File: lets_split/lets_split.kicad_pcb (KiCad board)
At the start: 2 copper layers, 114.2 x 82 mm, 76 parts, among them P1 USB-rewire, P2 USB_OTG, P3 WS2812, P4 TRRS jack, SW1 SW_PUSH, SW10 SW_PUSH, SW11 SW_PUSH, SW12 SW_PUSH, SW13 SW_PUSH, SW14 SW_PUSH, SW15 SW_PUSH, SW16 SW_PUSH, SW17 SW_PUSH, SW18 SW_PUSH, SW19 SW_PUSH, SW2 SW_PUSH, SW20 SW_PUSH, SW21 SW_PUSH, SW22 SW_PUSH, SW23 SW_PUSH, SW24 SW_PUSH, SW3 SW_PUSH, SW4 SW_PUSH, SW5 SW_PUSH, SW6 SW_PUSH, SW7 SW_PUSH, SW8 SW_PUSH, SW9 SW_PUSH, U1 ArduinoProMicro

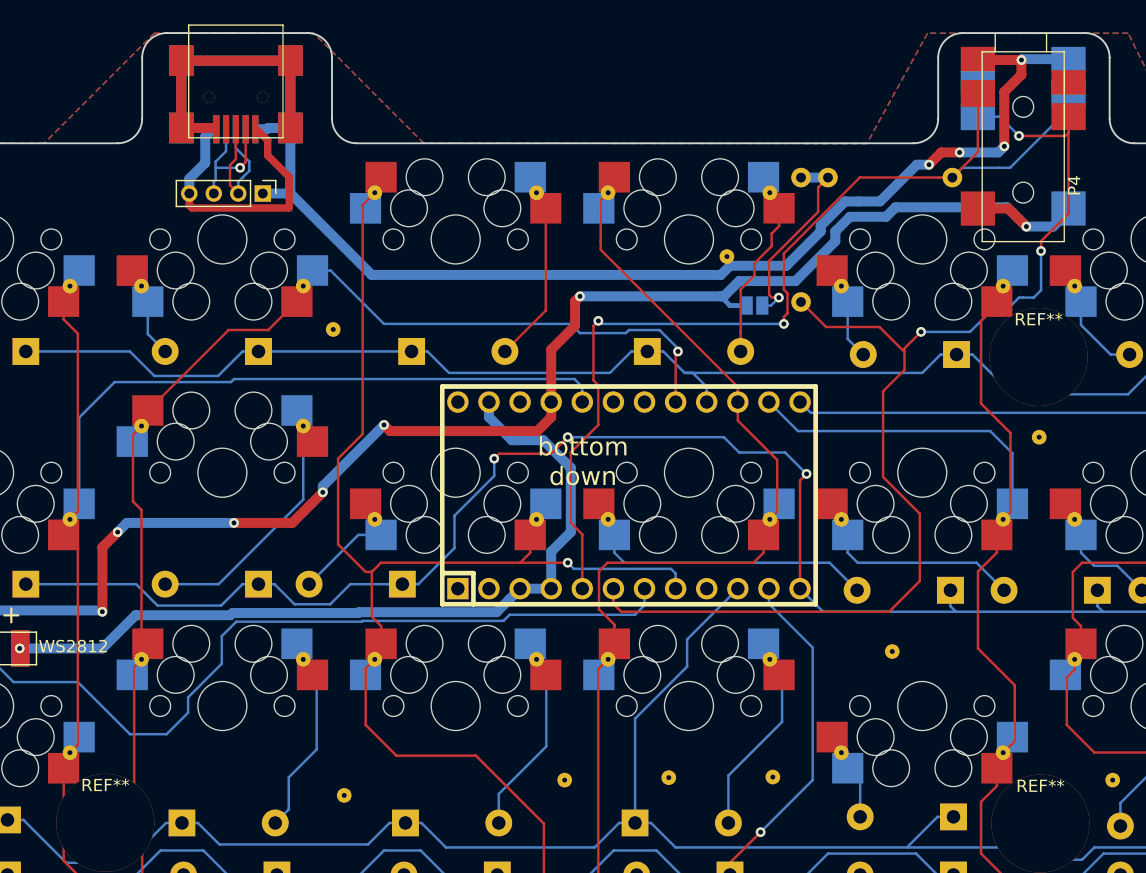
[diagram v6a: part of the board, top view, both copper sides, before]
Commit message: Updated schematic svg
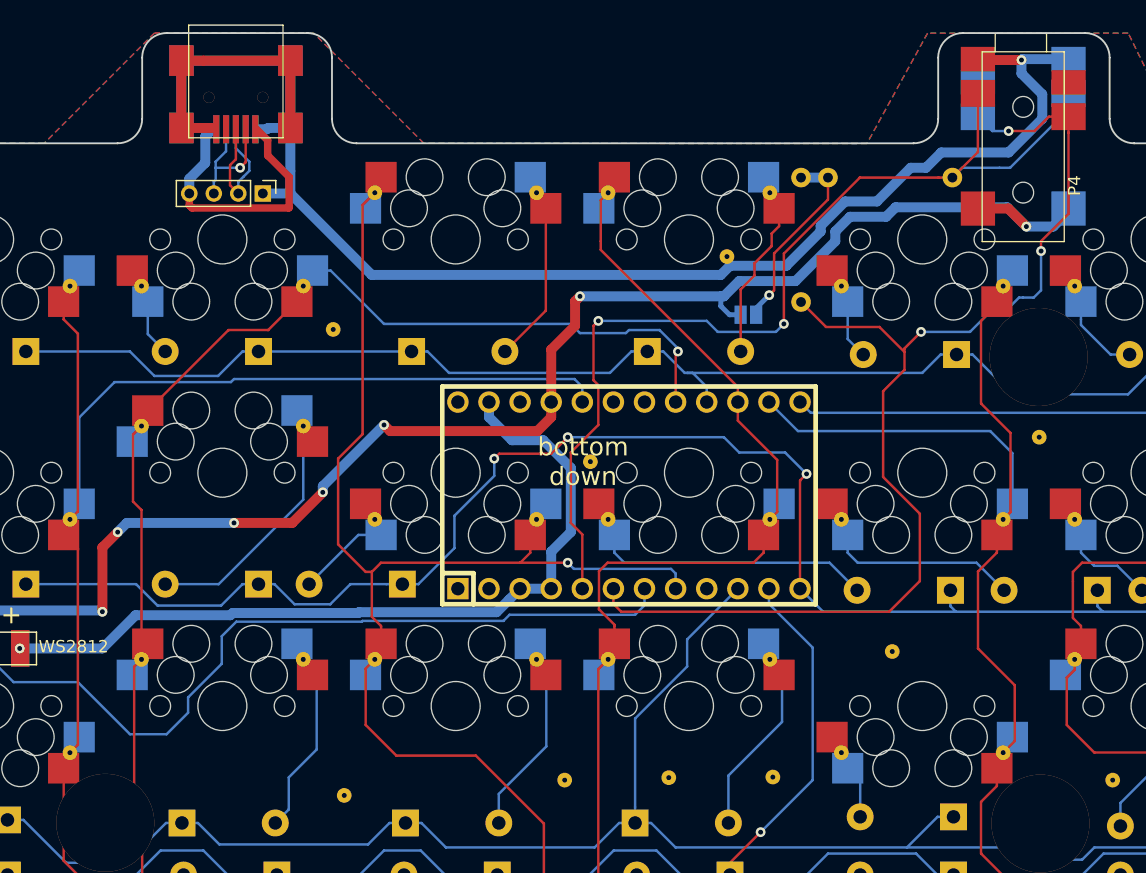
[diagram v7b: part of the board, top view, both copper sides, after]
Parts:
- added REF**: 1pin, Connect:1pin, F.Cu at (139.6, 91.0)
- moved JP1 0.90 mm to (152.5, 79.0)
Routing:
- net GND: track 199.1 -> 201.0 mm, vias 5 -> 2
- net VCC: track 124.1 -> 125.1 mm

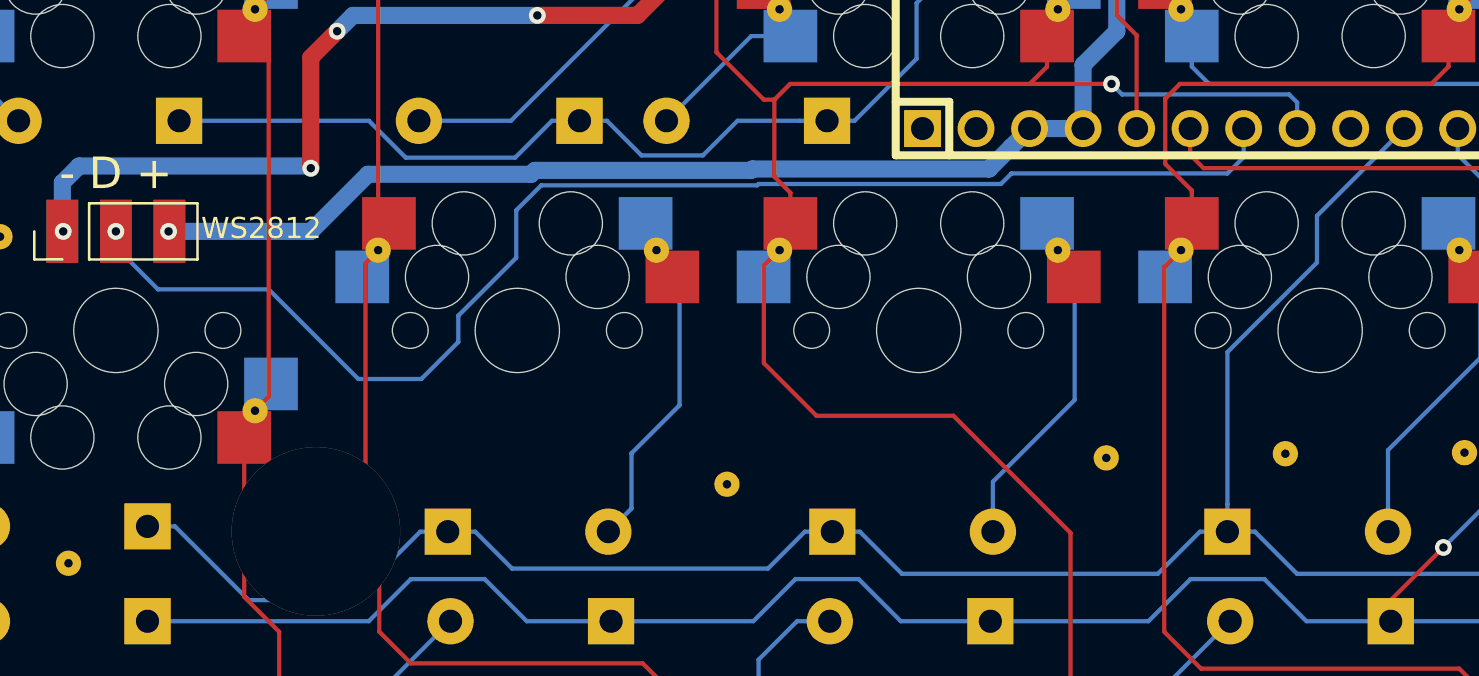
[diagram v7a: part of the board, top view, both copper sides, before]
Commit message: Added speaker output to the board
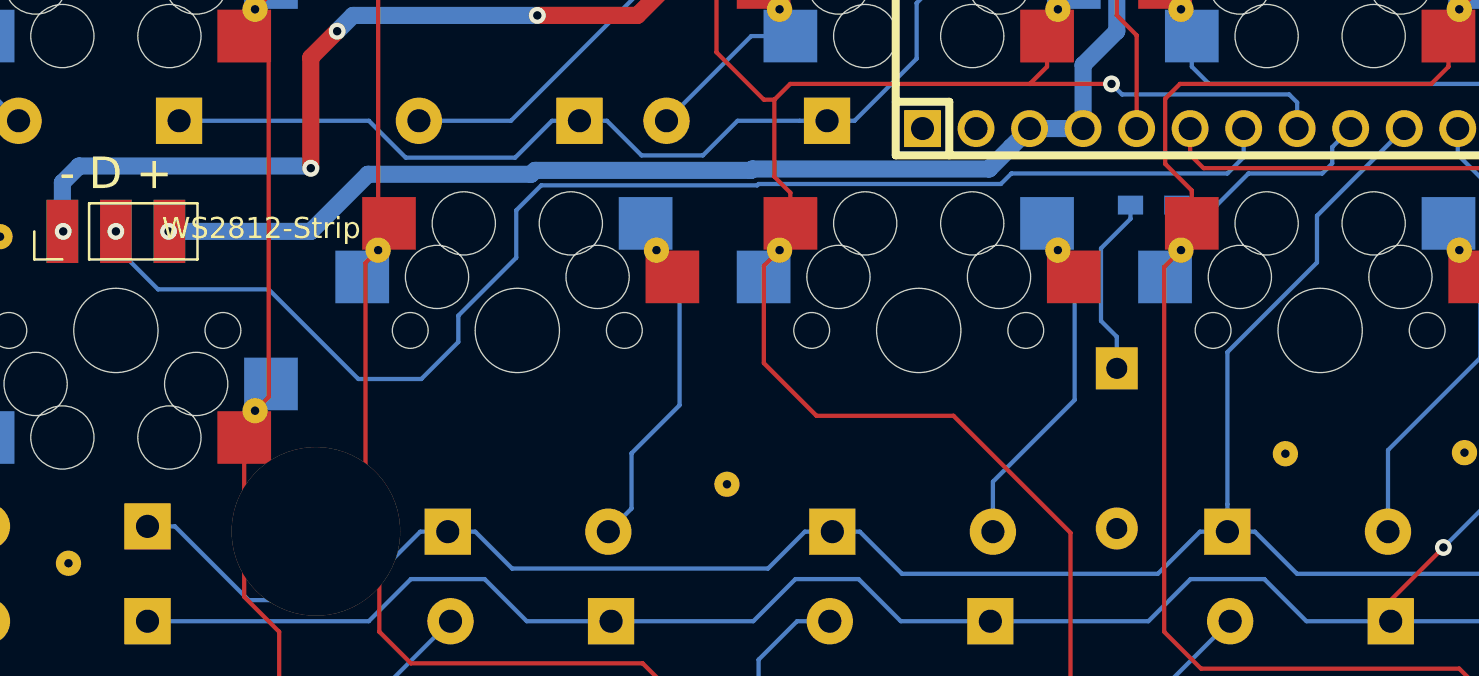
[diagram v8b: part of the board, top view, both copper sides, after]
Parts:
- removed the REF** at (137.5, 117.0)
- added J1: Speaker, Buzzers_Beepers:Buzzer_12x9.5RM7.6, B.Cu at (138.0, 112.8)
- added R3: 150, Resistors_SMD:R_0603_HandSoldering, B.Cu at (139.8, 105.0)
- P3: value WS2812 -> WS2812-Strip
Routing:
- net Net-(R3-Pad1): track 0.00 -> 10.2 mm
- net Net-(J1-Pad1): track 0.00 -> 8.64 mm
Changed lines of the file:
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@@
     (thickness 1.6)
     (drawings 33)
-    (tracks 781)
+    (tracks 792)
     (zones 0)
-    (modules 77)
-    (nets 53)
+    (modules 78)
+    (nets 54)
   )
   (page A4)
@@
   (net 47 /D-)
   (net 48 "Net-(P3-Pad2)")
-  (net 49 "Net-(U1-Pad9)")
-  (net 50 "Net-(U1-Pad18)")
-  (net 51 "Net-(P2-Pad4)")
-  (net 52 "Net-(P4-Pad6)")
+  (net 49 "Net-(U1-Pad18)")
+  (net 50 "Net-(P2-Pad4)")
+  (net 51 "Net-(P4-Pad6)")
+  (net 52 "Net-(J1-Pad1)")
+  (net 53 "Net-(R3-Pad1)")
   (net_class Default "This is the default net class."
     (clearance 0.2032)
@@
     (add_net "Net-(D8-Pad2)")
     (add_net "Net-(D9-Pad2)")
+    (add_net "Net-(J1-Pad1)")
     (add_net "Net-(JP1-Pad2)")
     (add_net "Net-(P1-Pad4)")
@@
     (add_net "Net-(P3-Pad2)")
     (add_net "Net-(P4-Pad6)")
+    (add_net "Net-(R3-Pad1)")
     (add_net "Net-(U1-Pad1)")
     (add_net "Net-(U1-Pad18)")
@@
     (add_net "Net-(U1-Pad22)")
     (add_net "Net-(U1-Pad24)")
-    (add_net "Net-(U1-Pad9)")
     (add_net SCL/D3)
     (add_net SDA)
@@
     (add_net row3)
   )
+  (module Buzzers_Beepers:Buzzer_12x9.5RM7.6 (layer B.Cu)
+    (at 138 112.75 270)
+    (descr "Generic Buzzer, D12mm height 9.5mm with RM7.6mm")
+    (tags buzzer)
+    (fp_text reference J1 (at 3.8 7.2 270) (layer B.SilkS)
+      (effects (font (size 1 1) (thickness 0.15)) (justify mirror))
+    )
+    (fp_text value Speaker (at 3.8 -7.4 270) (layer B.Fab)
+      (effects (font (size 1 1) (thickness 0.15)) (justify mirror))
+    )
+    (fp_circle (center 3.8 0) (end 9.9 0) (layer B.Fab) (width 0.12))
+    (fp_circle (center 3.8 0) (end 4.8 0) (layer B.Fab) (width 0.1))
+    (fp_circle (center 3.8 0) (end 9.8 0) (layer B.Fab) (width 0.1))
+    (fp_circle (center 3.8 0) (end 10.05 0) (layer B.CrtYd) (width 0.05))
+    (fp_text user %R (at 3.8 4 270) (layer B.Fab)
+      (effects (font (size 1 1) (thickness 0.15)) (justify mirror))
+    )
+    (fp_text user + (at -0.01 2.54 270) (layer B.SilkS)
+      (effects (font (size 1 1) (thickness 0.15)) (justify mirror))
+    )
+    (fp_text user + (at -0.01 2.54 270) (layer B.Fab)
+      (effects (font (size 1 1) (thickness 0.15)) (justify mirror))
+    )
+    (pad 2 thru_hole circle (at 7.6 0 270) (size 2 2) (drill 1) (layers *.Cu *.Mask)
+      (net 29 GND))
+    (pad 1 thru_hole rect (at 0 0 270) (size 2 2) (drill 1) (layers *.Cu *.Mask)
+      (net 52 "Net-(J1-Pad1)"))
+    (model ${KISYS3DMOD}/Buzzers_Beepers.3dshapes/Buzzer_12x9.5RM7.6.wrl
+      (at (xyz 0.15 0 0))
+      (scale (xyz 4 4 4))
+      (rotate (xyz 0 0 0))
+    )
+  )
   (module Connect:1pin (layer F.Cu)
     (at 139.6 91)
@@
       (net 29 GND))
     (pad 4 smd rect (at 0.8 -3.9 180) (size 0.5 2.3) (layers F.Cu F.Paste F.Mask)
-      (net 51 "Net-(P2-Pad4)"))
+      (net 50 "Net-(P2-Pad4)"))
     (pad 3 smd rect (at 0 -3.9 180) (size 0.5 2.3) (layers F.Cu F.Paste F.Mask)
       (net 46 /D+))
@@
       (net 37 SCL/D3))
     (pad 6 smd rect (at -5.25 -3.7 270) (size 2 2.8) (layers F.Cu F.Paste F.Mask)
-      (net 52 "Net-(P4-Pad6)"))
+      (net 51 "Net-(P4-Pad6)"))
     (pad 1 smd rect (at -7.15 3.7 270) (size 2 2.8) (layers F.Cu F.Paste F.Mask)
       (net 29 GND))
@@
       (effects (font (size 1 1) (thickness 0.15)))
     )
-    (fp_text value WS2812 (at 0.15 9.44 180) (layer F.SilkS)
+    (fp_text value WS2812-Strip (at 0.15 9.44 180) (layer F.SilkS)
       (effects (font (size 1 1) (thickness 0.15)))
     )
@@
   )
   (module Connect:1pin (layer F.Cu)
-    (at 137.5 117)
-    (descr "module 1 pin (ou trou mecanique de percage)")
-    (tags DEV)
-    (fp_text reference REF** (at 0 -1.397) (layer F.SilkS) hide
-      (effects (font (size 1 1) (thickness 0.15)))
-    )
-    (fp_text value 1pin (at 0 1.143) (layer F.Fab) hide
-      (effects (font (size 1 1) (thickness 0.15)))
-    )
-    (pad 1 thru_hole circle (at 0 0) (size 1.2 1.2) (drill 0.4) (layers *.Cu *.Mask F.SilkS)
-      (net 29 GND))
-  )
-  (module Connect:1pin (layer F.Cu)
     (at 146 116.8)
     (descr "module 1 pin (ou trou mecanique de percage)")
@@
       (net 33 col2))
     (pad 9 thru_hole circle (at 6.35 7.62) (size 1.7526 1.7526) (drill 1.0922) (layers *.Cu *.SilkS *.Mask)
-      (net 49 "Net-(U1-Pad9)"))
+      (net 53 "Net-(R3-Pad1)"))
     (pad 10 thru_hole circle (at 8.89 7.62) (size 1.7526 1.7526) (drill 1.0922) (layers *.Cu *.SilkS *.Mask)
       (net 6 row2))
@@
       (net 32 col1))
     (pad 18 thru_hole circle (at 1.27 -7.62) (size 1.7526 1.7526) (drill 1.0922) (layers *.Cu *.SilkS *.Mask)
-      (net 50 "Net-(U1-Pad18)"))
+      (net 49 "Net-(U1-Pad18)"))
     (pad 19 thru_hole circle (at -1.27 -7.62) (size 1.7526 1.7526) (drill 1.0922) (layers *.Cu *.SilkS *.Mask)
       (net 42 "Net-(U1-Pad19)"))
@@
       (net 29 GND))
   )
+  (module Resistors_SMD:R_0603_HandSoldering (layer B.Cu)
+    (at 139.75 105 180)
+    (descr "Resistor SMD 0603, hand soldering")
+    (tags "resistor 0603")
+    (attr smd)
+    (fp_text reference R3 (at 0.75 1.25) (layer B.SilkS)
+      (effects (font (size 1 1) (thickness 0.15)) (justify mirror))
+    )
+    (fp_text value 150 (at 0 -1.55 180) (layer B.Fab)
+      (effects (font (size 1 1) (thickness 0.15)) (justify mirror))
+    )
+    (fp_line (start 1.95 -0.7) (end -1.96 -0.7) (layer B.CrtYd) (width 0.05))
+    (fp_line (start 1.95 -0.7) (end 1.95 0.7) (layer B.CrtYd) (width 0.05))
+    (fp_line (start -1.96 0.7) (end -1.96 -0.7) (layer B.CrtYd) (width 0.05))
+    (fp_line (start -1.96 0.7) (end 1.95 0.7) (layer B.CrtYd) (width 0.05))
+    (fp_line (start -0.5 0.68) (end 0.5 0.68) (layer B.SilkS) (width 0.12))
+    (fp_line (start 0.5 -0.68) (end -0.5 -0.68) (layer B.SilkS) (width 0.12))
+    (fp_line (start -0.8 0.4) (end 0.8 0.4) (layer B.Fab) (width 0.1))
+    (fp_line (start 0.8 0.4) (end 0.8 -0.4) (layer B.Fab) (width 0.1))
+    (fp_line (start 0.8 -0.4) (end -0.8 -0.4) (layer B.Fab) (width 0.1))
+    (fp_line (start -0.8 -0.4) (end -0.8 0.4) (layer B.Fab) (width 0.1))
+    (fp_text user %R (at 0 0 180) (layer B.Fab)
+      (effects (font (size 0.4 0.4) (thickness 0.075)) (justify mirror))
+    )
+    (pad 2 smd rect (at 1.1 0 180) (size 1.2 0.9) (layers B.Cu B.Paste B.Mask)
+      (net 52 "Net-(J1-Pad1)"))
+    (pad 1 smd rect (at -1.1 0 180) (size 1.2 0.9) (layers B.Cu B.Paste B.Mask)
+      (net 53 "Net-(R3-Pad1)"))
+    (model ${KISYS3DMOD}/Resistors_SMD.3dshapes/R_0603.wrl
+      (at (xyz 0 0 0))
+      (scale (xyz 1 1 1))
+      (rotate (xyz 0 0 0))
+    )
+  )
+  (gr_text "LET'S SPLIT" (at 137.2 116.6) (layer B.SilkS)
+    (effects (font (size 5 5) (thickness 0.3)) (justify mirror))
+  )
   (gr_text "bottom\ndown" (at 139 91) (layer F.SilkS)
     (effects (font (size 1.5 1.5) (thickness 0.3)))
@@
     (effects (font (size 1.5 1.5) (thickness 0.3)))
   )
-  (gr_text "LET'S SPLIT" (at 137.2 116.6) (layer B.SilkS)
-    (effects (font (size 5 5) (thickness 0.3)) (justify mirror))
-  )
   (gr_line (start 105 56) (end 116.5 56) (layer Edge.Cuts) (width 0.15))
   (gr_arc (start 101 63) (end 103 63) (angle 90) (layer Edge.Cuts) (width 0.15))
@@
   (segment (start 132.5 104) (end 133 103.5) (width 0.2032) (layer B.Cu) (net 48))
   (segment (start 143.25 103.5) (end 144.02 102.73) (width 0.2032) (layer B.Cu) (net 48))
+  (segment (start 137.25 110.5) (end 138 111.25) (width 0.2032) (layer B.Cu) (net 52))
+  (segment (start 138 111.25) (end 138 112.75) (width 0.2032) (layer B.Cu) (net 52))
+  (segment (start 137.25 107.0532) (end 137.25 110.5) (width 0.2032) (layer B.Cu) (net 52))
+  (segment (start 138.65 105) (end 138.65 105.6532) (width 0.2032) (layer B.Cu) (net 52))
+  (segment (start 138.65 105.6532) (end 137.25 107.0532) (width 0.2032) (layer B.Cu) (net 52))
+  (segment (start 149.1 101.37) (end 148.223701 102.246299) (width 0.2032) (layer B.Cu) (net 53))
+  (segment (start 148.223701 102.246299) (end 148.223701 103.026299) (width 0.2032) (layer B.Cu) (net 53))
+  (segment (start 148.223701 103.026299) (end 147.75 103.5) (width 0.2032) (layer B.Cu) (net 53))
+  (segment (start 144.25 103.5) (end 147.75 103.5) (width 0.2032) (layer B.Cu) (net 53))
+  (segment (start 142.75 105) (end 144.25 103.5) (width 0.2032) (layer B.Cu) (net 53))
+  (segment (start 140.85 105) (end 142.75 105) (width 0.2032) (layer B.Cu) (net 53))
   (zone (net 29) (net_name GND) (layer F.Cu) (hatch edge 0.508)
     (priority 1)
